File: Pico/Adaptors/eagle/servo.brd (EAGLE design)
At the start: 34 x 24.1 mm, 4 parts

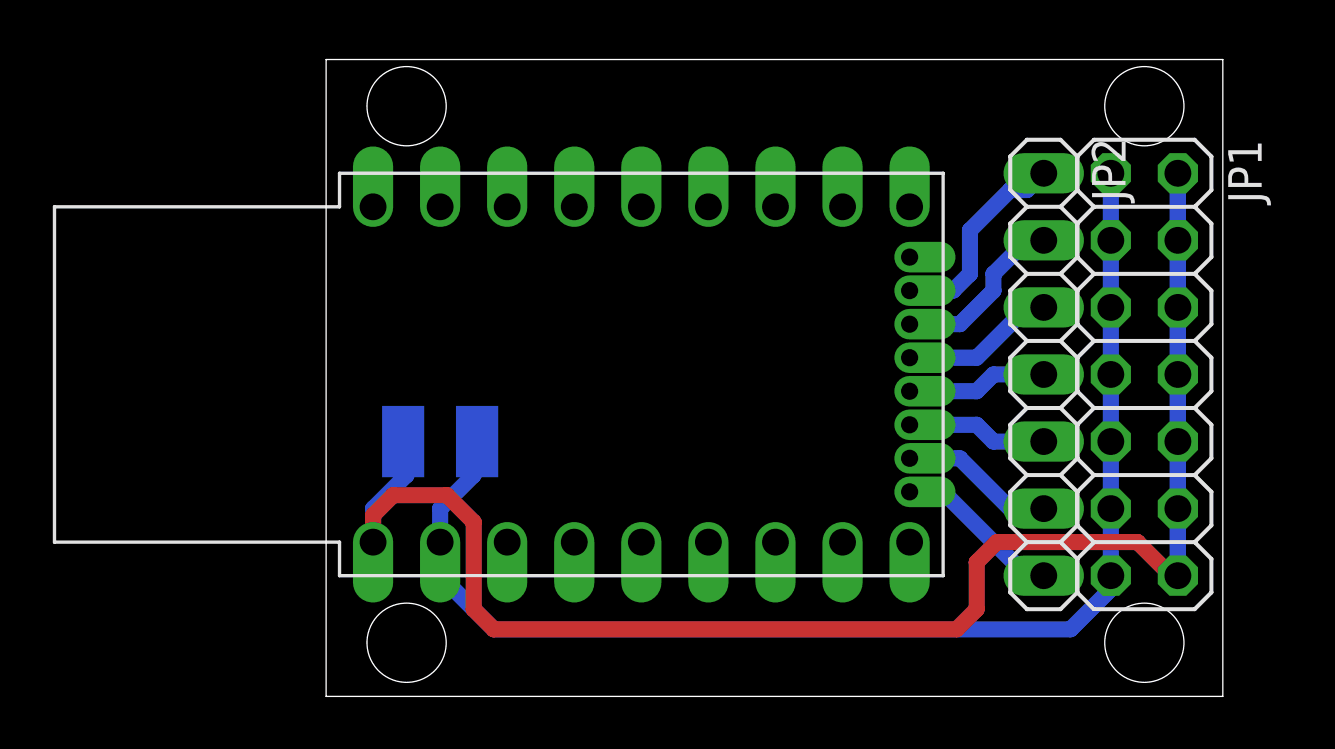
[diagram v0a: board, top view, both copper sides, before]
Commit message: nrf24 adaptor, and DRC
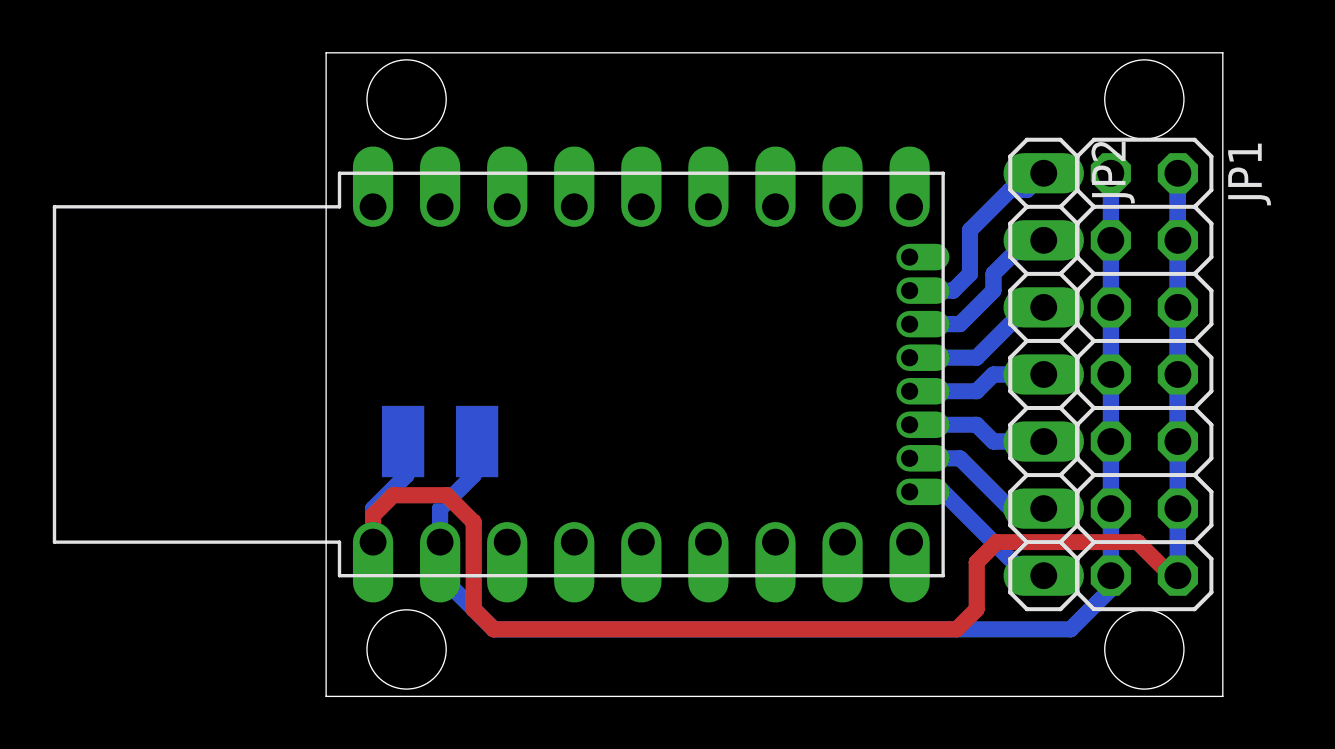
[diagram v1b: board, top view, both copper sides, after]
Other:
- board size 34 x 24.1 mm -> 34 x 24.4 mm
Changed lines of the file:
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@@
 <plain>
 <wire x1="0" y1="0" x2="33.96" y2="0" width="0" layer="20"/>
-<wire x1="33.96" y1="0" x2="33.96" y2="24.12" width="0" layer="20"/>
-<wire x1="33.96" y1="24.12" x2="0" y2="24.12" width="0" layer="20"/>
-<wire x1="0" y1="24.12" x2="0" y2="0" width="0" layer="20"/>
-<hole x="3.048" y="22.352" drill="3"/>
-<hole x="30.988" y="22.352" drill="3"/>
-<hole x="30.988" y="2.032" drill="3"/>
-<hole x="3.048" y="2.032" drill="3"/>
+<wire x1="33.96" y1="0" x2="33.96" y2="24.374" width="0" layer="20"/>
+<wire x1="33.96" y1="24.374" x2="0" y2="24.374" width="0" layer="20"/>
+<wire x1="0" y1="24.374" x2="0" y2="0" width="0" layer="20"/>
+<hole x="3.048" y="22.606" drill="3"/>
+<hole x="30.988" y="22.606" drill="3"/>
+<hole x="30.988" y="1.778" drill="3"/>
+<hole x="3.048" y="1.778" drill="3"/>
 </plain>
 <attributes>
@@
 </class>
 </classes>
-<designrules name="default *">
+<designrules name="oshpark-2layer">
 <description language="de">&lt;b&gt;EAGLE Design Rules&lt;/b&gt;
 &lt;p&gt;
@@
 Einstellungen hier und speichern die Design Rules unter
 einem neuen Namen ab.</description>
-<description language="en">&lt;b&gt;EAGLE Design Rules&lt;/b&gt;
+<description language="en">&lt;b&gt;Laen's PCB Order Design Rules&lt;/b&gt;
 &lt;p&gt;
-The default Design Rules have been set to cover
-a wide range of applications. Your particular design
-may have different requirements, so please make the
-necessary adjustments and save your customized
-design rules under a new name.</description>
+Please make sure your boards conform to these design rules.</description>
 <param name="layerSetup" value="(1*16)"/>
-<param name="mtCopper" value="0.035mm 0.035mm 0.035mm 0.035mm 0.035mm 0.035mm 0.035mm 0.035mm 0.035mm 0.035mm 0.035mm 0.035mm 0.035mm 0.035mm 0.035mm 0.035mm"/>
-<param name="mtIsolate" value="1.5mm 0.15mm 0.2mm 0.15mm 0.2mm 0.15mm 0.2mm 0.15mm 0.2mm 0.15mm 0.2mm 0.15mm 0.2mm 0.15mm 0.2mm"/>
+<param name="mtCopper" value="0.0356mm 0.0356mm 0.0356mm 0.0356mm 0.0356mm 0.0356mm 0.0356mm 0.0356mm 0.0356mm 0.0356mm 0.0356mm 0.0356mm 0.0356mm 0.0356mm 0.0356mm 0.0356mm"/>
+<param name="mtIsolate" value="1.5011mm 0.1499mm 0.2007mm 0.1499mm 0.2007mm 0.1499mm 0.2007mm 0.1499mm 0.2007mm 0.1499mm 0.2007mm 0.1499mm 0.2007mm 0.1499mm 0.2007mm"/>
 <param name="mdWireWire" value="6mil"/>
 <param name="mdWirePad" value="6mil"/>
@@
 <param name="mdViaViaSameLayer" value="8mil"/>
 <param name="mnLayersViaInSmd" value="2"/>
-<param name="mdCopperDimension" value="40mil"/>
-<param name="mdDrill" value="8mil"/>
+<param name="mdCopperDimension" value="15mil"/>
+<param name="mdDrill" value="6mil"/>
 <param name="mdSmdStop" value="0mil"/>
-<param name="msWidth" value="10mil"/>
-<param name="msDrill" value="24mil"/>
-<param name="msMicroVia" value="9.99mm"/>
+<param name="msWidth" value="6mil"/>
+<param name="msDrill" value="13mil"/>
+<param name="msMicroVia" value="13mil"/>
 <param name="msBlindViaRatio" value="0.5"/>
 <param name="rvPadTop" value="0.25"/>
@@
 <param name="rvMicroViaOuter" value="0.25"/>
 <param name="rvMicroViaInner" value="0.25"/>
-<param name="rlMinPadTop" value="10mil"/>
+<param name="rlMinPadTop" value="7mil"/>
 <param name="rlMaxPadTop" value="20mil"/>
-<param name="rlMinPadInner" value="10mil"/>
+<param name="rlMinPadInner" value="7mil"/>
 <param name="rlMaxPadInner" value="20mil"/>
-<param name="rlMinPadBottom" value="10mil"/>
+<param name="rlMinPadBottom" value="7mil"/>
 <param name="rlMaxPadBottom" value="20mil"/>
-<param name="rlMinViaOuter" value="8mil"/>
+<param name="rlMinViaOuter" value="7mil"/>
 <param name="rlMaxViaOuter" value="20mil"/>
-<param name="rlMinViaInner" value="8mil"/>
+<param name="rlMinViaInner" value="7mil"/>
 <param name="rlMaxViaInner" value="20mil"/>
 <param name="rlMinMicroViaOuter" value="4mil"/>
